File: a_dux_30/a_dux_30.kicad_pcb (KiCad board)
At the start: 2 copper layers, 118.2 x 97.9 mm, 34 parts

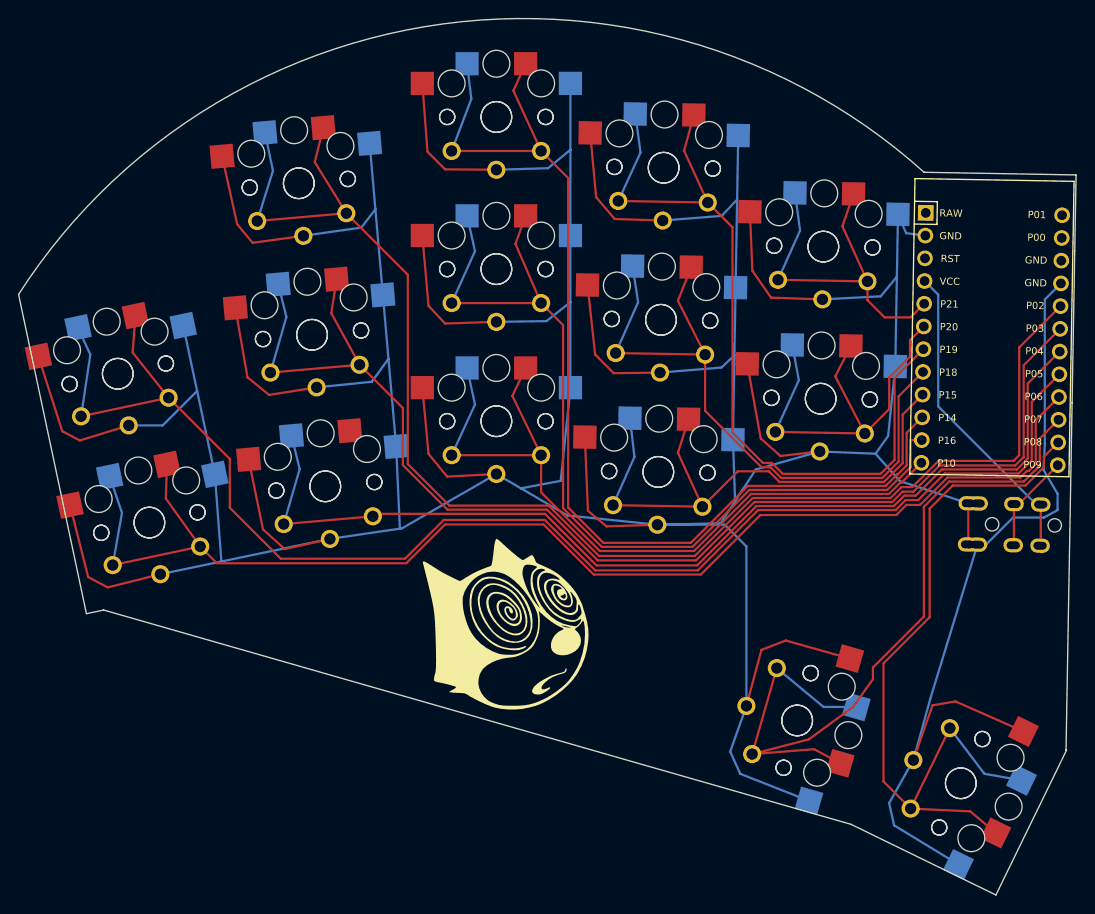
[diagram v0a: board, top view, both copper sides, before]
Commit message: add teardrops
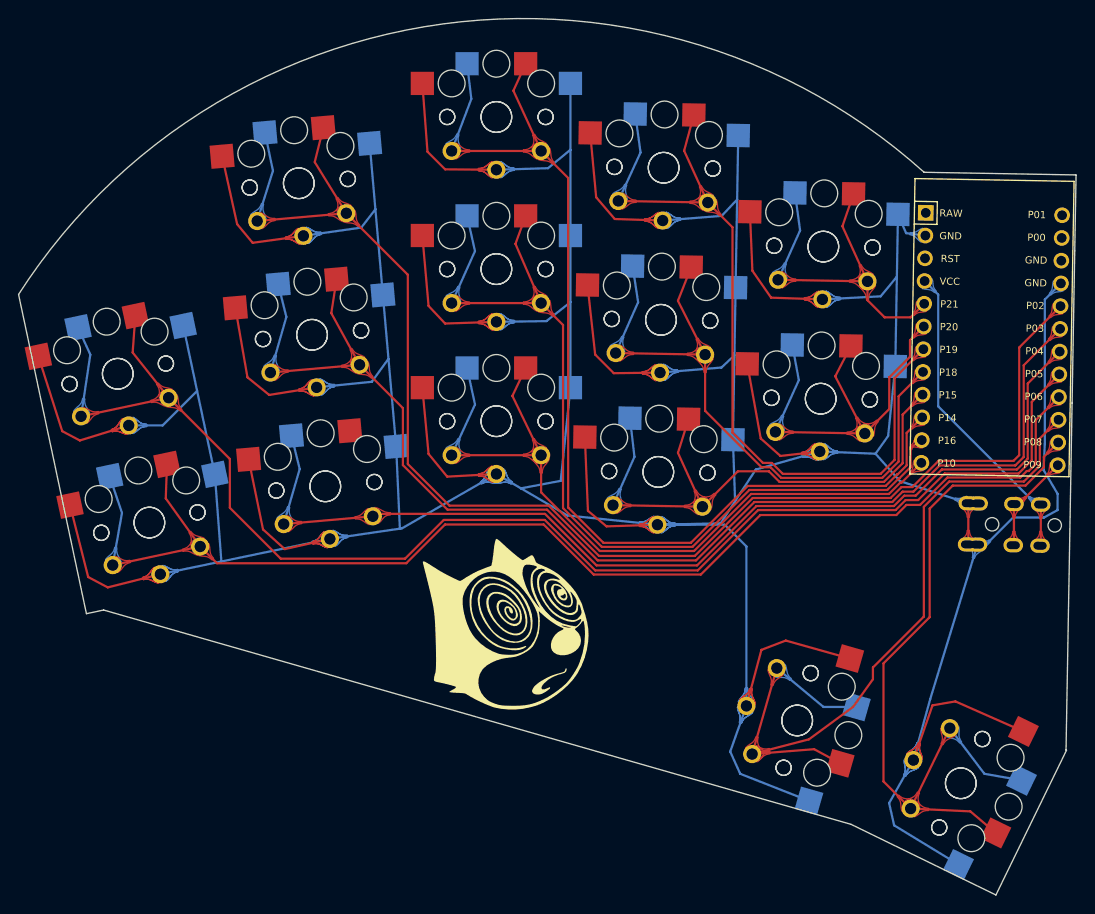
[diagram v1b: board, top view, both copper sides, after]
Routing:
- net P16: track 103.5 -> 102.9 mm

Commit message: add sketchy rounding/fillet
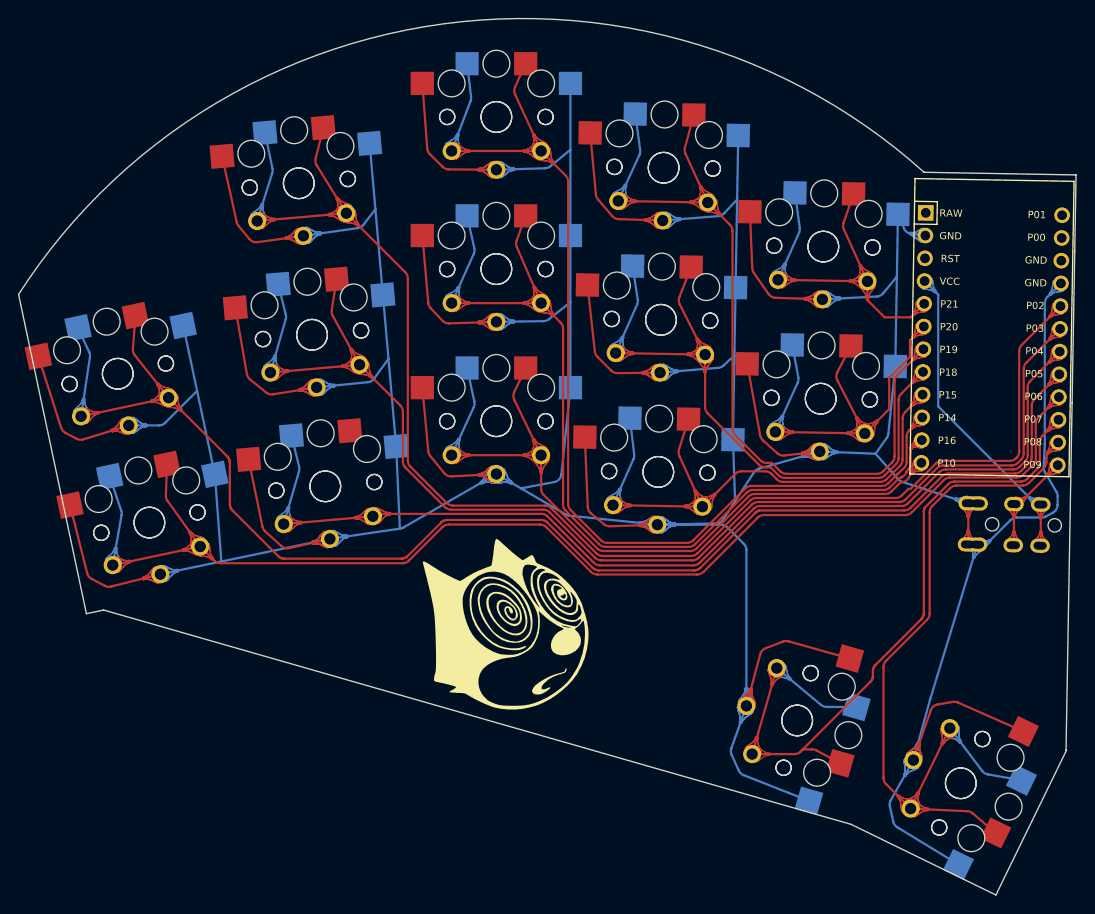
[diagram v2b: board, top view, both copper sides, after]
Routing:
- net P7: track 89.7 -> 84.3 mm
- net GND: track 738.5 -> 735.6 mm
- net P6: track 142.6 -> 141.9 mm
- net P5: track 158.1 -> 157.4 mm
- net P2: track 157.6 -> 157.0 mm
- net P3: track 138.4 -> 137.8 mm
